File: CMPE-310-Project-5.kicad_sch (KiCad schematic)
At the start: 8 parts, among them SW1 SW_Push, U1 8284, U4 8086_Min_Mode, Y1 Crystal

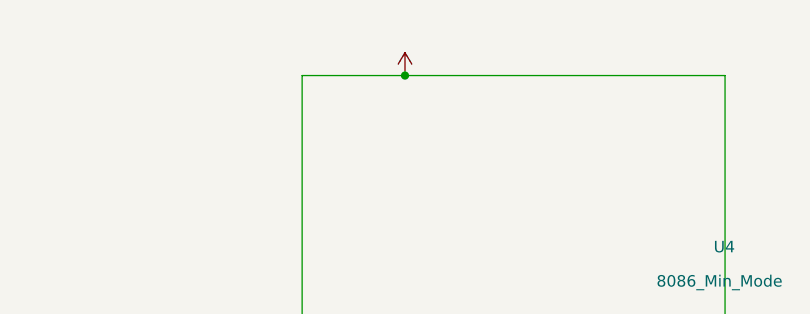
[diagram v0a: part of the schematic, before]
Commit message: Enabled inputs on the max235
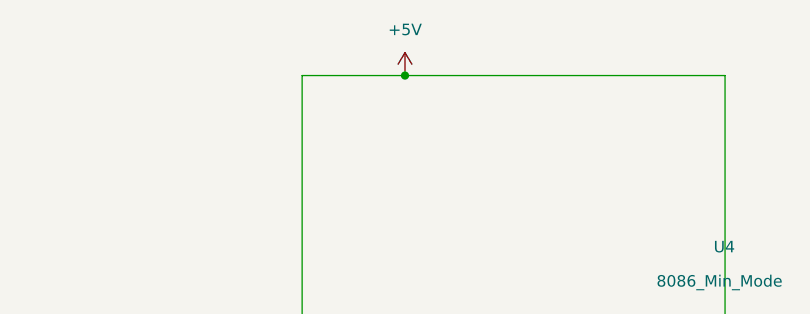
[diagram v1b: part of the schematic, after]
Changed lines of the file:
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@@
       (effects (font (size 1.27 1.27)) hide)
     )
-    (property "Value" "" (id 1) (at 60.96 24.13 0))
+    (property "Value" "+5V" (id 1) (at 60.96 24.13 0))
     (property "Footprint" "" (id 2) (at 60.96 29.21 0)
       (effects (font (size 1.27 1.27)) hide)
@@
       (reference "#PWR?") (unit 1) (value "+5V") (footprint "")
     )
+    (path "/87af81b5-cad9-406d-8283-65af2b602860/ed705d0b-56ef-479c-b140-27b7dd746870/3111651b-af1a-46fc-b47d-4f547787e7cc"
+      (reference "#PWR?") (unit 1) (value "+5V") (footprint "")
+    )
     (path "/cce1404b-fc30-47cc-b852-e0061990f2bb/3f9f7cc5-2cba-4e8a-bca1-3fa717e649ee"
       (reference "#PWR?") (unit 1) (value "GND") (footprint "")
@@
       (reference "#PWR?") (unit 1) (value "GND") (footprint "")
     )
+    (path "/87af81b5-cad9-406d-8283-65af2b602860/ed705d0b-56ef-479c-b140-27b7dd746870/69062c11-7347-4096-8151-5d07490a7074"
+      (reference "#PWR?") (unit 1) (value "+5V") (footprint "")
+    )
     (path "/65a0be0e-e533-4531-a6d7-d67f7f67ab34/75117201-9188-48a7-8212-64638d2ad3d8"
       (reference "#PWR?") (unit 1) (value "+5V") (footprint "")
@@
       (reference "#PWR?") (unit 1) (value "+5V") (footprint "")
     )
+    (path "/87af81b5-cad9-406d-8283-65af2b602860/ed705d0b-56ef-479c-b140-27b7dd746870/cd1cf589-f574-4945-bff1-6e7d61d209d0"
+      (reference "#PWR?") (unit 1) (value "GND") (footprint "")
+    )
     (path "/d26bc38b-e04e-43c9-b60f-cb1e6ddbb256"

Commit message: Updated PCB
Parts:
- added H? (x4): (no value), symbol Mechanical:MountingHole
- C1: value C -> (none); footprint Capacitor_SMD:CP_Elec_3x5.3 -> (none)
- D1: value DIODE -> (none); footprint Diode_SMD:D_0201_0603Metric -> (none)
- R1: value R -> (none); footprint Resistor_SMD:R_0201_0603Metric -> (none)
- R2: value 10k -> (none); footprint Resistor_SMD:R_0201_0603Metric -> (none)
- SW1: value SW_Push -> (none); footprint Button_Switch_Keyboard:SW_Cherry_MX_1.00u_PCB -> (none)
- U1: value 8284 -> (none); footprint Package_DIP:DIP-18_W7.62mm -> (none)
- U4: value 8086_Min_Mode -> (none); footprint Package_DIP:DIP-40_W15.24mm -> (none)
- Y1: value Crystal -> (none); footprint Crystal:Crystal_AT310_D3.0mm_L10.0mm_Horizontal -> (none)

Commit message: PCB wiring
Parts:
- C1: value (none) -> C; footprint (none) -> Capacitor_SMD:CP_Elec_3x5.3
- D1: value (none) -> DIODE; footprint (none) -> Diode_SMD:D_0201_0603Metric
- H? (x4): value (none) -> MountingHole
- R1: value (none) -> R; footprint (none) -> Resistor_SMD:R_0201_0603Metric
- R2: value (none) -> 10k; footprint (none) -> Resistor_SMD:R_0201_0603Metric
- SW1: value (none) -> SW_Push; footprint (none) -> Button_Switch_Keyboard:SW_Cherry_MX_1.00u_PCB
- U1: value (none) -> 8284; footprint (none) -> Package_DIP:DIP-18_W7.62mm
- U4: value (none) -> 8086_Min_Mode; footprint (none) -> Package_DIP:DIP-40_W15.24mm
- Y1: value (none) -> Crystal; footprint (none) -> Crystal:Crystal_AT310_D3.0mm_L10.0mm_Horizontal
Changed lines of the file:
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@@
       (effects (font (size 1.27 1.27)) (justify right))
     )
-    (property "Value" "" (id 1) (at 36.83 134.6199 90)
+    (property "Value" "DIODE" (id 1) (at 36.83 134.6199 90)
       (effects (font (size 1.27 1.27)) (justify right))
     )
-    (property "Footprint" "" (id 2) (at 33.02 133.35 0)
+    (property "Footprint" "Diode_SMD:D_0201_0603Metric" (id 2) (at 33.02 133.35 0)
       (effects (font (size 1.27 1.27)) hide)
     )
@@
     (in_bom yes) (on_board yes) (fields_autoplaced)
     (property "Reference" "SW1" (id 0) (at 54.61 132.08 0))
-    (property "Value" "" (id 1) (at 54.61 134.62 0))
-    (property "Footprint" "" (id 2) (at 54.61 134.62 0)
+    (property "Value" "SW_Push" (id 1) (at 54.61 134.62 0))
+    (property "Footprint" "Button_Switch_Keyboard:SW_Cherry_MX_1.00u_PCB" (id 2) (at 54.61 134.62 0)
       (effects (font (size 1.27 1.27)) hide)
     )
@@
       (effects (font (size 1.27 1.27)) (justify left))
     )
-    (property "Value" "" (id 1) (at 71.12 137.1599 0)
-      (effects (font (size 1.27 1.27)) (justify left))
-    )
-    (property "Footprint" "" (id 2) (at 66.802 135.89 90)
+    (property "Value" "10k" (id 1) (at 71.12 137.1599 0)
+      (effects (font (size 1.27 1.27)) (justify left))
+    )
+    (property "Footprint" "Resistor_SMD:R_0201_0603Metric" (id 2) (at 66.802 135.89 90)
       (effects (font (size 1.27 1.27)) hide)
     )
@@
       (effects (font (size 1.27 1.27)) (justify left))
     )
-    (property "Value" "" (id 1) (at 48.26 134.6199 0)
-      (effects (font (size 1.27 1.27)) (justify left))
-    )
-    (property "Footprint" "" (id 2) (at 43.942 133.35 90)
+    (property "Value" "R" (id 1) (at 48.26 134.6199 0)
+      (effects (font (size 1.27 1.27)) (justify left))
+    )
+    (property "Footprint" "Resistor_SMD:R_0201_0603Metric" (id 2) (at 43.942 133.35 90)
       (effects (font (size 1.27 1.27)) hide)
     )
@@
       (effects (font (size 1.27 1.27)) (justify left))
     )
-    (property "Value" "" (id 1) (at 51.5494 78.74 0)
-      (effects (font (size 1.27 1.27)) (justify left))
-    )
-    (property "Footprint" "" (id 2) (at 49.53 99.06 0)
+    (property "Value" "8284" (id 1) (at 51.5494 78.74 0)
+      (effects (font (size 1.27 1.27)) (justify left))
+    )
+    (property "Footprint" "Package_DIP:DIP-18_W7.62mm" (id 2) (at 49.53 99.06 0)
       (effects (font (size 1.27 1.27) italic) hide)
     )
@@
       (effects (font (size 1.27 1.27)) (justify left))
     )
-    (property "Value" "" (id 1) (at 24.13 191.7699 0)
+    (property "Value" "MountingHole" (id 1) (at 24.13 191.7699 0)
       (effects (font (size 1.27 1.27)) (justify left))
     )
@@
       (effects (font (size 1.27 1.27)) (justify right))
     )
-    (property "Value" "" (id 1) (at 68.58 113.0299 90)
+    (property "Value" "Crystal" (id 1) (at 68.58 113.0299 90)
       (effects (font (size 1.27 1.27)) (justify right))
     )
-    (property "Footprint" "" (id 2) (at 64.77 111.76 0)
+    (property "Footprint" "Crystal:Crystal_AT310_D3.0mm_L10.0mm_Horizontal" (id 2) (at 64.77 111.76 0)
       (effects (font (size 1.27 1.27)) hide)
     )
@@
       (effects (font (size 1.27 1.27)) (justify left))
     )
-    (property "Value" "" (id 1) (at 38.1 149.8599 0)
-      (effects (font (size 1.27 1.27)) (justify left))
-    )
-    (property "Footprint" "" (id 2) (at 33.02 148.59 0)
+    (property "Value" "C" (id 1) (at 38.1 149.8599 0)
+      (effects (font (size 1.27 1.27)) (justify left))
+    )
+    (property "Footprint" "Capacitor_SMD:CP_Elec_3x5.3" (id 2) (at 33.02 148.59 0)
       (effects (font (size 1.27 1.27)) hide)
     )
@@
       (effects (font (size 1.27 1.27)) (justify left))
     )
-    (property "Value" "" (id 1) (at 280.67 163.8299 0)
+    (property "Value" "MountingHole" (id 1) (at 280.67 163.8299 0)
       (effects (font (size 1.27 1.27)) (justify left))
     )
@@
       (effects (font (size 1.27 1.27)) (justify left))
     )
-    (property "Value" "" (id 1) (at 22.86 25.3999 0)
+    (property "Value" "MountingHole" (id 1) (at 22.86 25.3999 0)
       (effects (font (size 1.27 1.27)) (justify left))
     )
@@
       (effects (font (size 1.27 1.27)) (justify left))
     )
-    (property "Value" "" (id 1) (at 88.9 52.07 0)
-      (effects (font (size 1.27 1.27)) (justify left))
-    )
-    (property "Footprint" "" (id 2) (at 97.79 99.06 0)
+    (property "Value" "8086_Min_Mode" (id 1) (at 88.9 52.07 0)
+      (effects (font (size 1.27 1.27)) (justify left))
+    )
+    (property "Footprint" "Package_DIP:DIP-40_W15.24mm" (id 2) (at 97.79 99.06 0)
       (effects (font (size 1.27 1.27) italic) hide)
     )
@@
       (effects (font (size 1.27 1.27)) (justify left))
     )
-    (property "Value" "" (id 1) (at 281.94 24.1299 0)
-      (effects (font (size 1.27 1.27)) (justify left))
-    )
+    (property "Value" "MountingHole" (id 1) (at 281.94 24.1299 0)
+      (effects (font (size 1.27 1.27)) (justify left))
+    )

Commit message: Another change
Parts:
- gave numbers to parts that had none: 4
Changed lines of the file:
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@@
   (symbol (lib_id "Mechanical:MountingHole") (at 21.59 190.5 0) (unit 1)
     (in_bom yes) (on_board yes) (fields_autoplaced)
-    (property "Reference" "H?" (id 0) (at 24.13 189.2299 0)
+    (property "Reference" "H2" (id 0) (at 24.13 189.2299 0)
       (effects (font (size 1.27 1.27)) (justify left))
     )
@@
   (symbol (lib_id "Mechanical:MountingHole") (at 278.13 162.56 0) (unit 1)
     (in_bom yes) (on_board yes) (fields_autoplaced)
-    (property "Reference" "H?" (id 0) (at 280.67 161.2899 0)
+    (property "Reference" "H3" (id 0) (at 280.67 161.2899 0)
       (effects (font (size 1.27 1.27)) (justify left))
     )
@@
   (symbol (lib_id "Mechanical:MountingHole") (at 20.32 24.13 0) (unit 1)
     (in_bom yes) (on_board yes) (fields_autoplaced)
-    (property "Reference" "H?" (id 0) (at 22.86 22.8599 0)
+    (property "Reference" "H1" (id 0) (at 22.86 22.8599 0)
       (effects (font (size 1.27 1.27)) (justify left))
     )
@@
   (symbol (lib_id "Mechanical:MountingHole") (at 279.4 22.86 0) (unit 1)
     (in_bom yes) (on_board yes) (fields_autoplaced)
-    (property "Reference" "H?" (id 0) (at 281.94 21.5899 0)
+    (property "Reference" "H4" (id 0) (at 281.94 21.5899 0)
       (effects (font (size 1.27 1.27)) (justify left))
     )
@@
       (reference "DS1") (unit 1) (value "LCD4x20") (footprint "parts:LCD4x20")
     )
+    (path "/c7009550-b21f-4d0a-8ae9-710a510907c6"
+      (reference "H1") (unit 1) (value "MountingHole") (footprint "")
+    )
     (path "/9ae1249b-3cd5-4b56-8152-fc5a2ed8e84b"
-      (reference "H?") (unit 1) (value "MountingHole") (footprint "")
+      (reference "H2") (unit 1) (value "MountingHole") (footprint "")
     )
     (path "/aa7ddcaf-40f6-47b9-b614-053507653447"
-      (reference "H?") (unit 1) (value "MountingHole") (footprint "")
-    )
-    (path "/c7009550-b21f-4d0a-8ae9-710a510907c6"
-      (reference "H?") (unit 1) (value "MountingHole") (footprint "")
+      (reference "H3") (unit 1) (value "MountingHole") (footprint "")
     )
     (path "/e95a6420-e0e2-4379-8d24-250c82b541f5"
-      (reference "H?") (unit 1) (value "MountingHole") (footprint "")
+      (reference "H4") (unit 1) (value "MountingHole") (footprint "")
     )
     (path "/65a0be0e-e533-4531-a6d7-d67f7f67ab34/663809f0-cda7-4438-9ef6-bd03b342e9a5"
